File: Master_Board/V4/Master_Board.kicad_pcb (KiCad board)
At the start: 2 copper layers, 137.4 x 98.3 mm, 204 parts, among them J101 649016227222, J201 Header_Male_Pin_2.54mm_1X3_,_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, J202 Header_Male_Pin_2.54mm_1X6_,_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, J301 Header_Male_Pin_2.54mm_1X2_,_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, J401 649006227222, J701 649004227222, J702 649004227222, J703 649004227222, J704 649002227222, J801 649002227222, J802 649002227222, J901 649002227222, J902 649002227222, J903 649002227222, J904 649002227222, Q1101 BSS806NH6327XTSA1, Q1102 BSS806NH6327XTSA1, Q1103 BSS806NH6327XTSA1, Q701 BC849BLT1G, Q702 BC849BLT1G, Q703 BC849BLT1G, Q704 BC849BLT1G, Q801 BC849BLT1G, Q802 BC849BLT1G, SW201 PTS645SM43SMTR92, SW202 PTS645SM43SMTR92, U201 STM32F446RE, U301 OKI-78SR-5/1.5-W36-C, U302 AZ1117IH-3.3TRG1, U401 SN65HVD232DR, U501 SN65HVD232DR, U701 CPC1117NTR, U901 ACPL-C87A-500E, U902 NCS1S2405SC, U903 ACPL-C87A-500E, U904 LMV321RILT, U905 LMV321RILT

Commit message: Reparation of the fan circuit -no more patch require on the PSU
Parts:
- removed R1101, R1103, R1105: RC0805JR-074K7L, Resistors:R0805
- removed R1102, R1104, R1106: RC0805JR-07100KL, Resistors:R0805
- moved Q1101 1.27 mm to (110.2, 47.0), turned to 0 degrees
- moved Q1102 1.10 mm to (104.1, 47.0), turned to 0 degrees
- moved Q1103 1.10 mm to (98.0, 47.0), turned to 0 degrees
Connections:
- Q1101 pad 2: DGND -> /IO5
- Q1101 pad 3: /IO5 -> 12V
- Q1102 pad 2: DGND -> /IO7
- Q1102 pad 3: /IO7 -> 12V
- Q1103 pad 2: DGND -> /IO8
- Q1103 pad 3: /IO8 -> 12V
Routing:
- net DGND: track 687.9 -> 655.6 mm, vias 26 -> 25
- net 12V: track 152.2 -> 161.7 mm, vias 4 -> 2
- net /PC0: track 50.5 -> 48.4 mm
- net /IO5: track 36.4 -> 37.7 mm
- net /PC1: track 50.2 -> 51.3 mm
- net /IO7: track 35.2 -> 36.2 mm
- net /PC2: track 60.1 -> 60.8 mm

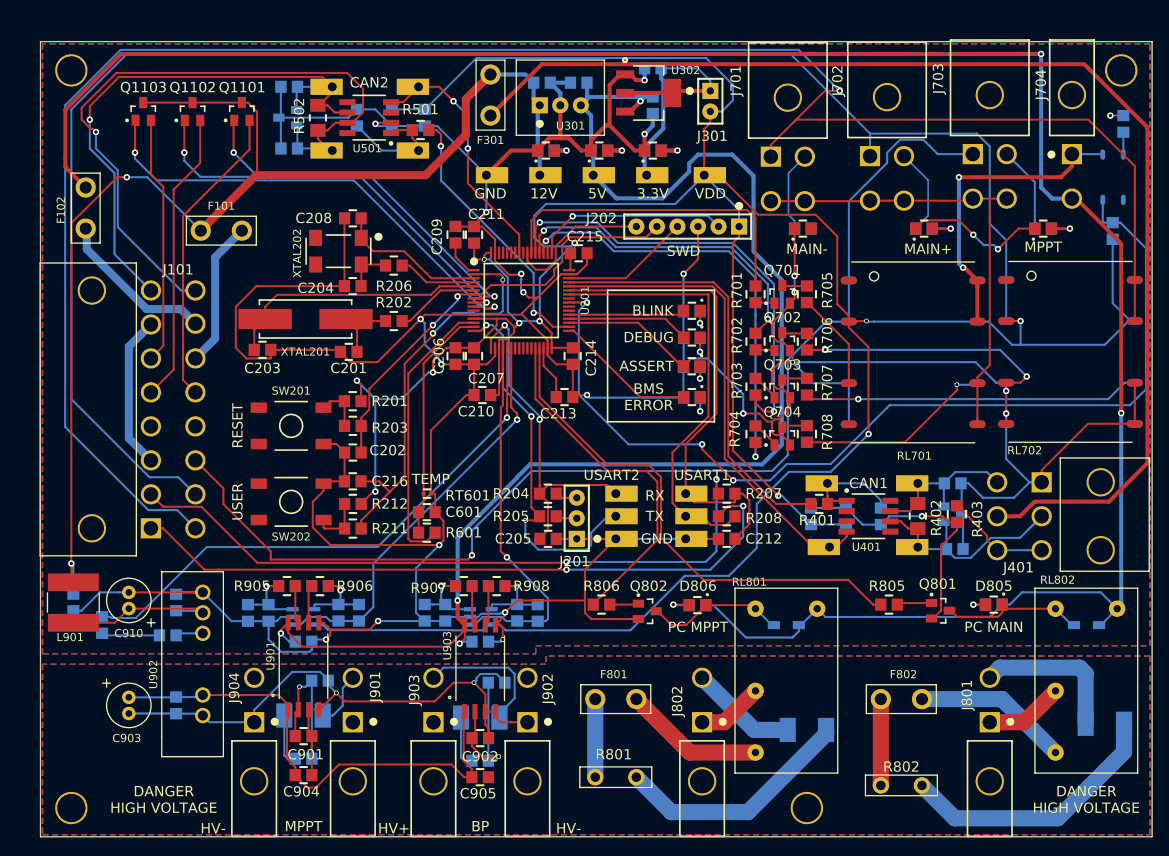
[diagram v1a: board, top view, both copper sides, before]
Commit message: Master V4 routed
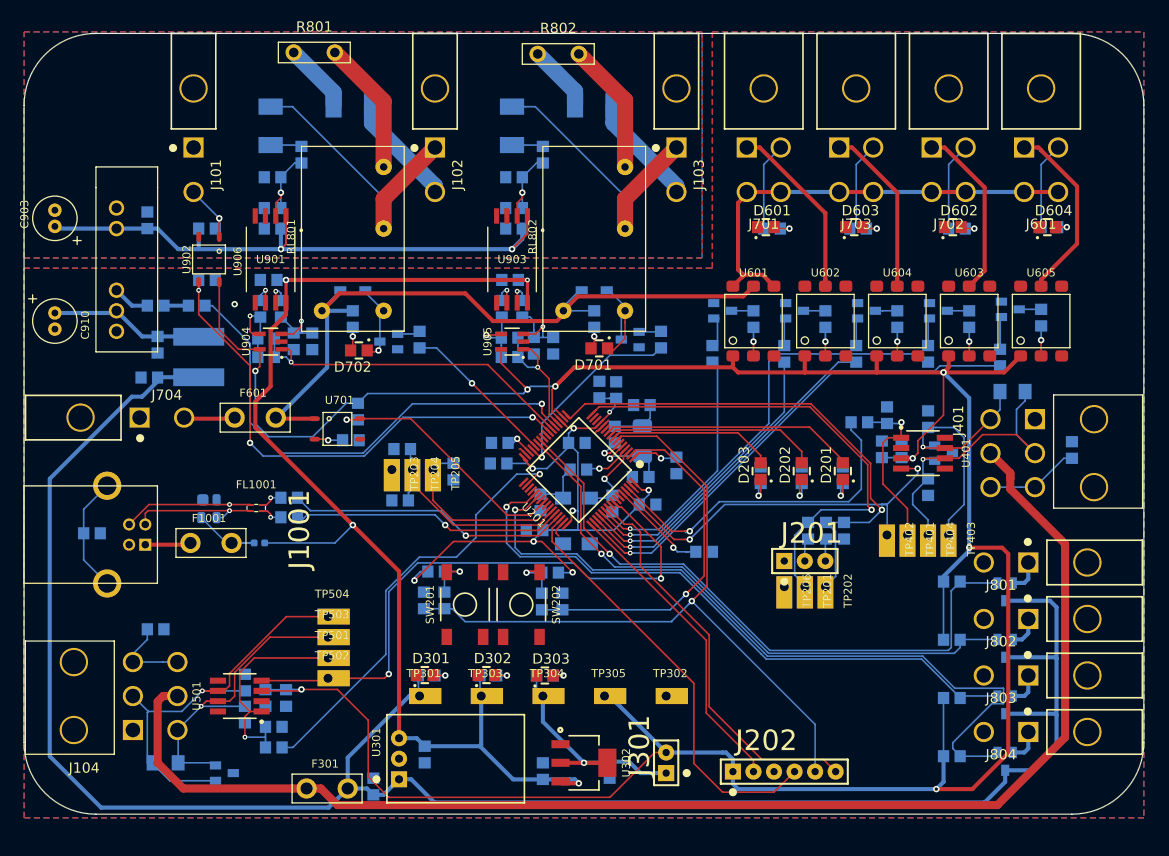
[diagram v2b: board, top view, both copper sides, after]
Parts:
- removed C601: 885012107015, Capacitors:C0805
- removed D703, D805, D806: 150080VS75000, Diodes:LED_0805_GREEN
- removed F101: 39505000440, Fuses:TE5_395
- removed F102: 39511000440, Fuses:TE5_395
- removed F801, F802: 80812000440, Fuses:TE5_395
- removed the G*** at (120.1, 75.4)
- removed J901, J902, J903, J904: 649002227222, Connectors:649002227222
- removed REF** (x4): Mounting_Hole_3mm, Connectors:Mounting_Hole_3mm
- removed RL701, RL702, RL703, RL704: CPC1907B, Relays:CPC1907B
- removed RT601: NCP15WB473F03RC, Resistors:R0402
- added D601: 150080BS75000, Diodes:LED_0805_BLUE, F.Cu at (174.0, 61.3)
- added D602: 150080BS75000, Diodes:LED_0805_BLUE, F.Cu at (197.1, 61.3)
- added D603: 150080BS75000, Diodes:LED_0805_BLUE, F.Cu at (184.9, 61.3)
- added D604: 150080BS75000, Diodes:LED_0805_BLUE, F.Cu at (208.8, 61.3)
- added F1001: 39505000440, Fuses:TE5_395, F.Cu at (106.4, 100.3)
- added F601: 39511000440, Fuses:TE5_395, F.Cu at (111.9, 84.8)
- added FB1001: 742792605, Filter:FB0603, B.Cu at (111.8, 100.3)
- added FL1001: 744230900, Filter:744230900, F.Cu at (112.0, 96.0)
- added G***: LOGO, Logo:Eclipse_logo_small_Metal, F.Cu at (184.7, 116.9)
- added J1001: 61400416121, Connectors:61400416121, F.Cu at (98.3, 98.0)
- added J102: 649002227222, Connectors:649002227222, F.Cu at (134.1, 44.1)
- added J103: 649002227222, Connectors:649002227222, F.Cu at (164.0, 44.1)
- added J104: 649006227222, Connectors:649006227222, F.Cu at (89.5, 119.3)
- added J601: 649004227222, Connectors:649004227222, F.Cu at (209.0, 44.1)
- added J803: 649002227222, Connectors:649002227222, F.Cu at (214.8, 116.7)
- added J804: 649002227222, Connectors:649002227222, F.Cu at (214.8, 123.7)
- added Q601: BC849BLT1G, IC:SOT-23-3, B.Cu at (205.2, 71.4)
- added Q803: BSS806NH6327XTSA1, IC:SOT-23-3, B.Cu at (204.6, 127.3)
- added R1002: RC0805JR-0710KL, Resistors:R0805, B.Cu at (197.0, 105.1)
- added R1003: RC0805JR-0710KL, Resistors:R0805, B.Cu at (197.0, 112.3)
- added R1004: RC0805JR-0710KL, Resistors:R0805, B.Cu at (197.0, 119.5)
- added R1005: RC0805JR-070RL, Resistors:R0805, B.Cu at (115.1, 97.2)
- added R1006: RC0805JR-070RL, Resistors:R0805, B.Cu at (115.1, 94.7)
- added R101: RC0805JR-070RL, Resistors:R0805, B.Cu at (98.6, 111.0)
- added R214: RC0805JR-0710KL, Resistors:R0805, B.Cu at (168.4, 101.4)
- added R602: RC0805FR-071K1L, Resistors:R0805, B.Cu at (209.0, 71.4)
- added R603: RC0805JR-071KL, Resistors:R0805, B.Cu at (209.0, 61.3)
- added R807: RC0805JR-0710KL, Resistors:R0805, B.Cu at (197.0, 126.7)
- added R914: RC0805JR-074K7L, Resistors:R0805, B.Cu at (104.9, 61.5)
- added R915: RC0805JR-074K7L, Resistors:R0805, B.Cu at (104.9, 67.8)
- added U601: TLP3543A(TP1,F, IC:6-SMD, F.Cu at (173.5, 72.9)
- added U602: TLP3543A(TP1,F, IC:6-SMD, F.Cu at (182.4, 72.9)
- added U603: TLP3543A(TP1,F, IC:6-SMD, F.Cu at (200.2, 72.9)
- added U604: TLP3543A(TP1,F, IC:6-SMD, F.Cu at (191.3, 72.9)
- added U605: TLP3543A(TP1,F, IC:6-SMD, F.Cu at (209.0, 72.9)
- added U906: CPC1117NTR, IC:4-SOP, F.Cu at (106.2, 65.3)
- C201, C202, C203, C204, C205, C206, C207, C208, C209, C210, C211, C212, C213, C214, C215, C216, C901, C902, C904, C905, L901, Q1101, Q1102, Q1103, Q701, Q702, Q703, Q704, Q801, Q802, R201, R202, R203, R204, R205, R206, R207, R208, R211, R212, R401, R402, R403, R501, R502, R701, R702, R703, R704, R705, R706, R707, R708, R805, R806, R905, R906, R907, R908, XTAL202: moved to B.Cu
- D1001: value 150080RS75000 -> 8240026; footprint Diodes:LED_0805_RED -> Diodes:SOT-143-4; moved to B.Cu
- D301, D302, D303, D701, D702: value 150080VS75000 -> 150080BS75000; footprint Diodes:LED_0805_GREEN -> Diodes:LED_0805_BLUE
- J101: value 649016227222 -> 649002227222; footprint Connectors:649016227222 -> Connectors:649002227222
- R1001: value RC0805JR-07330RL -> RC0805JR-070RL
- R601: value RC0805JR-0733KL -> RC0805JR-0710KL; moved to B.Cu
- U301: value OKI-78SR-5/1.5-W36-C -> OKI-78SR-5_1.5-W36H-C; footprint Assembly:OKI-78SR_Vertical -> Assembly:OKI-78SR_Horizontal
- U701, U904, U905: moved to F.Cu
- XTAL201: value ABLS-8.000MHZ-D-T -> 7A-8.000MAHJ-T; footprint Crystals:HC49_US -> Crystals:TXC_7A_Series; moved to B.Cu
- moved Q1103 129.4 mm to (204.6, 120.3)
- moved J704 128.9 mm to (90.3, 84.8), turned to 270 degrees
- moved Q1102 120.4 mm to (204.6, 113.4)
- moved Q1101 111.5 mm to (204.6, 106.4)
- moved R712 103.8 mm to (122.7, 87.6), turned to 0 degrees
- moved U701 100.8 mm to (122.0, 86.2), turned to 0 degrees
- moved R802 99.9 mm to (149.4, 39.9), turned to 0 degrees
- moved D802 99.1 mm to (153.8, 46.2), turned to 0 degrees
- moved R801 97.0 mm to (119.2, 39.7), turned to 0 degrees
- moved R713 95.5 mm to (124.6, 83.1), turned to 270 degrees
- moved D801 95.5 mm to (124.0, 46.2), turned to 0 degrees
- moved C301 88.7 mm to (126.5, 129.4), turned to 270 degrees
- moved F301 88.1 mm to (120.8, 130.7), turned to 0 degrees
- moved C304 87.9 mm to (155.7, 129.4), turned to 90 degrees
- moved C302 86.0 mm to (132.8, 127.5), turned to 90 degrees
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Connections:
- net /Voltage Sense/5V_ISO renamed 5V_HP
- D1001 pad 1: Net-(D1001-Pad1) -> DGND
- D1001 pad 2: /PB12 -> (no net)
- D201 pad 2: /PC6 -> /PC2
- D202 pad 2: /PB15 -> /PC1
- D203 pad 2: /PB14 -> /PC0
- D701 pad 1: DGND -> Net-(D701-Pad1)
- D702 pad 1: DGND -> Net-(D702-Pad1)
- D801 pad 2: Net-(D801-Pad2) -> /HV_Mppt+
- D802 pad 2: Net-(D802-Pad2) -> /HV_High_Side+
- D803 pad 1: /Contactor_12V -> /12V_Mush
- D803 pad 2: Net-(D803-Pad2) -> Net-(D701-Pad1)
- D804 pad 1: /Contactor_12V -> /12V_Mush
- D804 pad 2: Net-(D804-Pad2) -> Net-(D702-Pad1)
- D901 pad 2: Net-(D901-Pad2) -> /HV_Mppt-
- D902 pad 2: Net-(D902-Pad2) -> /HV_High_Side-
- J101 pad 1: /RS232_TX -> AGND
- J101 pad 2: /RS232_RX -> /HV_Low_Side+
- J101 pad 3: /GND -> (no net)
- J701 pad 1: /IO2 -> Net-(J701-Pad1)
- J702 pad 1: /IO1 -> Net-(J702-Pad1)
- J703 pad 1: /IO3 -> Net-(J703-Pad1)
- J704 pad 1: /ContactorControl/12V_Protected -> DGND
- J704 pad 2: /Contactor_12V -> Net-(F601-Pad1)
- J801 pad 2: Net-(D802-Pad2) -> DGND
- J802 pad 2: Net-(D801-Pad2) -> DGND
- Q1101 pad 1: /PC0 -> /PB0
- Q1101 pad 2: /IO5 -> Net-(J801-Pad1)
- Q1102 pad 1: /PC1 -> /PB1
- Q1102 pad 2: /IO7 -> Net-(J802-Pad1)
- Q1103 pad 1: /PC2 -> /PC6
- Q1103 pad 2: /IO8 -> Net-(J803-Pad1)
- Q801 pad 3: Net-(D803-Pad2) -> Net-(D701-Pad1)
- Q802 pad 3: Net-(D804-Pad2) -> Net-(D702-Pad1)
- R1001 pad 1: DGND -> /USB/Shield_Connector
- R1001 pad 2: Net-(D1001-Pad1) -> DGND
- R401 pad 1: /PA12 -> /PB9
- R601 pad 1: /NTC_1_ADC -> /PA15
- R601 pad 2: /NTC_1_GPIO -> Net-(Q601-Pad1)
- R709 pad 2: Net-(D701-Pad2) -> Net-(D601-Pad2)
- R710 pad 2: Net-(D702-Pad2) -> Net-(D602-Pad2)
- R801 pad 2: Net-(F801-Pad1) -> Net-(R801-Pad2)
- R802 pad 2: Net-(F802-Pad1) -> Net-(R802-Pad2)
- R803 pad 1: /Contactor_12V -> /12V_Mush
- R803 pad 2: Net-(D805-Pad2) -> Net-(D701-Pad2)
- R804 pad 1: /Contactor_12V -> /12V_Mush
- R804 pad 2: Net-(D806-Pad2) -> Net-(D702-Pad2)
- RL801 pad 1: /Contactor_12V -> /12V_Mush
- RL801 pad 2: Net-(D804-Pad2) -> Net-(D702-Pad1)
- RL801 pad 3: Net-(J802-Pad1) -> /HV_Mppt-
- RL801 pad 4: Net-(F801-Pad2) -> Net-(R801-Pad2)
- RL802 pad 1: /Contactor_12V -> /12V_Mush
- RL802 pad 2: Net-(D803-Pad2) -> Net-(D701-Pad1)
- RL802 pad 3: Net-(J801-Pad1) -> /HV_High_Side-
- RL802 pad 4: Net-(F802-Pad2) -> Net-(R802-Pad2)
- TP402 pad 1: /PA11 -> /PB8
- U201 pad 14: /NTC_1_GPIO -> /PA0
- U201 pad 15: /NTC_1_ADC -> /PA1
- U401 pad 4: /PA11 -> /PB8
- U701 pad 1: /ContactorControl/12V_Protected -> /12V_Mush
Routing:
- net DGND: track 655.6 -> 8.39 mm, vias 25 -> 1
- net /Contactor_12V: track 268.3 -> 0.00 mm, vias 2 -> 0
- net /IO2: track 238.2 -> 0.00 mm, vias 1 -> 0
- net /IO1: track 202.4 -> 0.00 mm
- net /IO3: track 143.3 -> 0.00 mm, vias 1 -> 0
- net /12V_Mush: track 0.00 -> 93.5 mm
- net /PC7: track 0.00 -> 92.8 mm, vias 0 -> 1
- net /PC9: track 120.5 -> 31.4 mm, vias 3 -> 1
- net 12V: track 161.7 -> 248.4 mm, vias 2 -> 0
- net /RS232_RX: track 84.8 -> 0.00 mm, vias 2 -> 0
- net /RS232_TX: track 84.5 -> 0.00 mm, vias 2 -> 0
- net AGND: track 80.5 -> 0.00 mm, vias 2 -> 0
- net /PB0: track 0.00 -> 78.1 mm, vias 0 -> 1
- net /PB1: track 0.00 -> 72.2 mm, vias 0 -> 1
- net /PA7: track 0.00 -> 64.2 mm, vias 0 -> 3
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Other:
- board size 137.4 x 98.3 mm -> 138.4 x 96.5 mm
- board text removed: "(c) 2018 - Eclipse X"
- board text removed: "12V"
- board text removed: "3.3V"
- board text removed: "5V"
- board text removed: "ASSERT"
- board text removed: "BLINK"
- board text removed: "BMS ERROR"
- board text removed: "BMS Master Board V3"
- board text removed: "BP"
- board text removed: "CAN1"
- board text removed: "CAN2"
- board text removed: "DANGER HIGH VOLTAGE"
- board text removed: "DEBUG"
- board text removed: "GND"
- board text removed: "HV+"
- board text removed: "HV-"
- board text removed: "Julien Bourassa/Pierre-Olivier Meilleur"
- board text removed: "MAIN+"
- board text removed: "MAIN-"
- board text removed: "MPPT"
- board text removed: "PC MAIN"
- board text removed: "PC MPPT"
- board text removed: "RESET"
- board text removed: "RX"
- board text removed: "SWD"
- board text removed: "TEMP"
- board text removed: "TX"
- board text removed: "USART1"
- board text removed: "USART2"
- board text removed: "USER"
- board text removed: "VDD"

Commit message: Repair USB ESD protection net
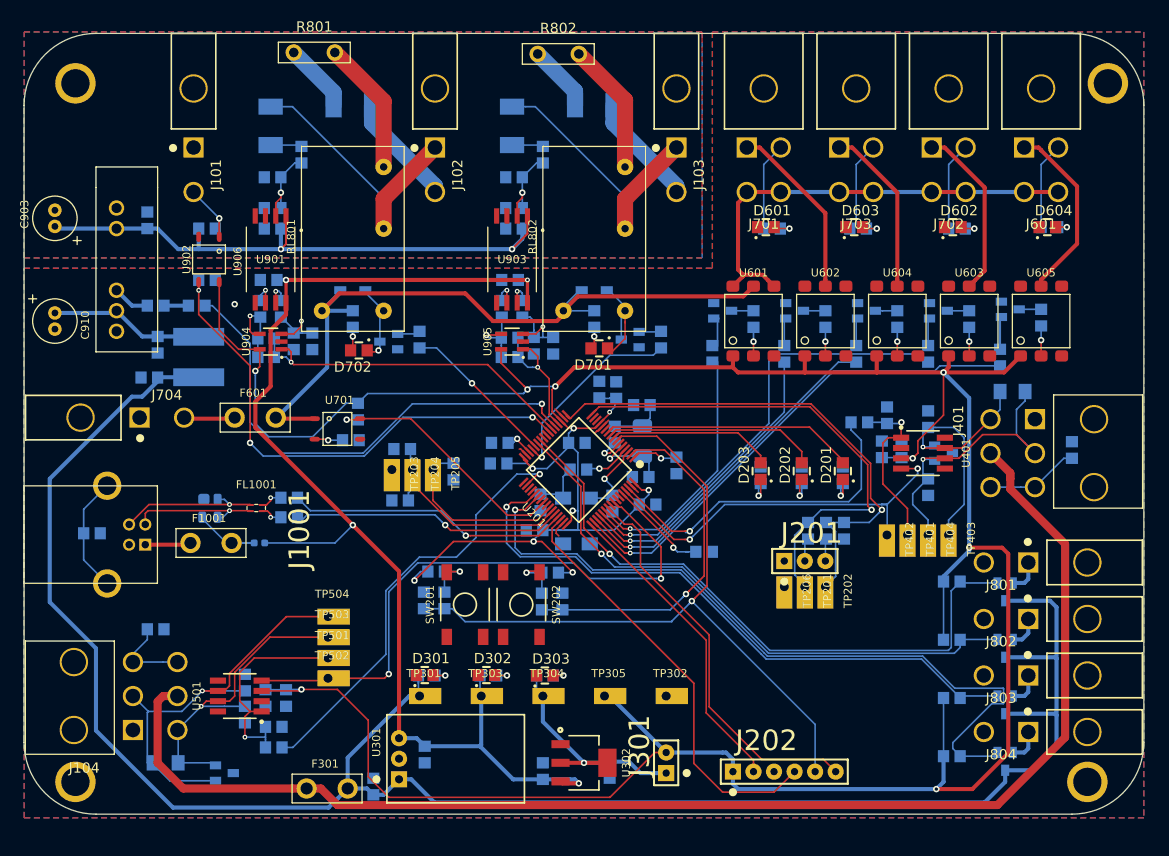
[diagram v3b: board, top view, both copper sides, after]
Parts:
- added H101: Mounting-Hole-M3, Connectors:Mounting_Hole_3mm, F.Cu at (214.8, 129.9)
- added H102: Mounting-Hole-M3, Connectors:Mounting_Hole_3mm, F.Cu at (89.7, 129.9)
- added H103: Mounting-Hole-M3, Connectors:Mounting_Hole_3mm, F.Cu at (217.3, 43.5)
- added H104: Mounting-Hole-M3, Connectors:Mounting_Hole_3mm, F.Cu at (89.7, 43.5)
- moved D1001 0.14 mm to (105.5, 94.9)
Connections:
- D1001 pad 2: (no net) -> /USB/D+
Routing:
- net 12V: track 248.4 -> 243.2 mm
- net /USB/D+: track 16.7 -> 18.4 mm
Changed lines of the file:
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@@
     (thickness 1.6)
     (drawings 8)
-    (tracks 1207)
+    (tracks 1211)
     (zones 0)
-    (modules 212)
-    (nets 172)
+    (modules 216)
+    (nets 176)
   )
   (page A4)
@@
   (net 170 "Net-(D701-Pad1)")
   (net 171 "Net-(D702-Pad1)")
+  (net 172 "Net-(H101-Pad1)")
+  (net 173 "Net-(H102-Pad1)")
+  (net 174 "Net-(H103-Pad1)")
+  (net 175 "Net-(H104-Pad1)")
   (net_class Default "Ceci est la Netclass par défaut"
     (clearance 0.1524)
@@
     (add_net "Net-(FL1001-Pad2)")
     (add_net "Net-(FL1001-Pad3)")
+    (add_net "Net-(H101-Pad1)")
+    (add_net "Net-(H102-Pad1)")
+    (add_net "Net-(H103-Pad1)")
+    (add_net "Net-(H104-Pad1)")
     (add_net "Net-(J601-Pad1)")
     (add_net "Net-(J601-Pad2)")
@@
     )
   )
-  (module Diodes:SOT-143-4 (layer B.Cu)
-    (at 105.41 94.996)
-    (fp_text reference D1001 (at 1.905 3.81) (layer B.SilkS)
-      (effects (font (size 1 1) (thickness 0.15)) (justify mirror))
-    )
-    (fp_text value 8240026 (at 1.27 5.08) (layer B.Fab)
-      (effects (font (size 1 1) (thickness 0.15)) (justify mirror))
-    )
-    (fp_circle (center 0 -1.27) (end 0.1 -1.27) (layer B.SilkS) (width 0.3))
-    (pad 4 smd roundrect (at -0.2 2.2) (size 1 1.4) (layers B.Cu B.Paste B.Mask) (roundrect_rratio 0.25)
-      (net 137 "Net-(D1001-Pad4)"))
-    (pad 3 smd roundrect (at 1.7 2.2) (size 1 1.4) (layers B.Cu B.Paste B.Mask) (roundrect_rratio 0.25)
-      (net 141 /USB/D-))
-    (pad 2 smd roundrect (at 1.7 0) (size 1 1.4) (layers B.Cu B.Paste B.Mask) (roundrect_rratio 0.25))
-    (pad 1 smd roundrect (at 0 0) (size 1.4 1.4) (layers B.Cu B.Paste B.Mask) (roundrect_rratio 0.25)
-      (net 1 DGND))
-    (model ${KISYS3DMOD}/Diodes/SOT143-4L.stp
-      (offset (xyz 0.75 1 0.5))
-      (scale (xyz 1 1 1))
-      (rotate (xyz 0 0 0))
-    )
-  )
   (module Crystals:TXC_7A_Series (layer B.Cu)
     (at 159.749164 87.731638 90)
@@
       (xy 0.952035 0.4064) (xy 1.036532 0.406546)) (layer F.Mask) (width 0.01))
   )
+  (module Connectors:Mounting_Hole_3mm (layer F.Cu)
+    (at 214.757 129.868184)
+    (fp_text reference H101 (at 0 -3.302) (layer F.SilkS) hide
+      (effects (font (size 1.27 1.27) (thickness 0.2032)))
+    )
+    (fp_text value Mounting-Hole-M3 (at 0 3.683) (layer F.Fab) hide
+      (effects (font (size 1.27 1.27) (thickness 0.2032)))
+    )
+    (pad 1 thru_hole circle (at 0 0) (size 5 5) (drill 3.5) (layers *.Cu *.Mask)
+      (net 172 "Net-(H101-Pad1)"))
+  )
+  (module Connectors:Mounting_Hole_3mm (layer F.Cu)
+    (at 89.662 129.868184)
+    (fp_text reference H102 (at 0 -3.302) (layer F.SilkS) hide
+      (effects (font (size 1.27 1.27) (thickness 0.2032)))
+    )
+    (fp_text value Mounting-Hole-M3 (at 0 3.683) (layer F.Fab) hide
+      (effects (font (size 1.27 1.27) (thickness 0.2032)))
+    )
+    (pad 1 thru_hole circle (at 0 0) (size 5 5) (drill 3.5) (layers *.Cu *.Mask)
+      (net 173 "Net-(H102-Pad1)"))
+  )
+  (module Connectors:Mounting_Hole_3mm (layer F.Cu)
+    (at 217.297 43.508184)
+    (fp_text reference H103 (at 0 -3.302) (layer F.SilkS) hide
+      (effects (font (size 1.27 1.27) (thickness 0.2032)))
+    )
+    (fp_text value Mounting-Hole-M3 (at 0 3.683) (layer F.Fab) hide
+      (effects (font (size 1.27 1.27) (thickness 0.2032)))
+    )
+    (pad 1 thru_hole circle (at 0 0) (size 5 5) (drill 3.5) (layers *.Cu *.Mask)
+      (net 174 "Net-(H103-Pad1)"))
+  )
+  (module Connectors:Mounting_Hole_3mm (layer F.Cu)
+    (at 89.662 43.508184)
+    (fp_text reference H104 (at 0 -3.302) (layer F.SilkS) hide
+      (effects (font (size 1.27 1.27) (thickness 0.2032)))
+    )
+    (fp_text value Mounting-Hole-M3 (at 0 3.683) (layer F.Fab) hide
+      (effects (font (size 1.27 1.27) (thickness 0.2032)))
+    )
+    (pad 1 thru_hole circle (at 0 0) (size 5 5) (drill 3.5) (layers *.Cu *.Mask)
+      (net 175 "Net-(H104-Pad1)"))
+  )
+  (module Diodes:SOT-143-4 (layer B.Cu)
+    (at 105.537 94.943184)
+    (fp_text reference D1001 (at 1.905 3.81) (layer B.SilkS)
+      (effects (font (size 1 1) (thickness 0.15)) (justify mirror))
+    )
+    (fp_text value 8240026 (at 1.27 5.08) (layer B.Fab)
+      (effects (font (size 1 1) (thickness 0.15)) (justify mirror))
+    )
+    (fp_circle (center 0 -1.27) (end 0.1 -1.27) (layer B.SilkS) (width 0.3))
+    (pad 1 smd roundrect (at 0 0) (size 1.4 1.4) (layers B.Cu B.Paste B.Mask) (roundrect_rratio 0.25)
+      (net 1 DGND))
+    (pad 2 smd roundrect (at 1.7 0) (size 1 1.4) (layers B.Cu B.Paste B.Mask) (roundrect_rratio 0.25)
+      (net 142 /USB/D+))
+    (pad 3 smd roundrect (at 1.7 2.2) (size 1 1.4) (layers B.Cu B.Paste B.Mask) (roundrect_rratio 0.25)
+      (net 141 /USB/D-))
+    (pad 4 smd roundrect (at -0.2 2.2) (size 1 1.4) (layers B.Cu B.Paste B.Mask) (roundrect_rratio 0.25)
+      (net 137 "Net-(D1001-Pad4)"))
+    (model ${KISYS3DMOD}/Diodes/SOT143-4L.stp
+      (offset (xyz 0.75 1 0.5))
+      (scale (xyz 1 1 1))
+      (rotate (xyz 0 0 0))
+    )
+  )
   (gr_arc (start 212.852 124.968) (end 212.852 133.858) (angle -90) (layer Edge.Cuts) (width 0.1))
   (gr_arc (start 92.202 124.968) (end 83.312 124.968) (angle -90) (layer Edge.Cuts) (width 0.1))
@@
   (segment (start 210.947 125.423184) (end 210.947 121.613184) (width 0.508) (layer B.Cu) (net 13))
   (segment (start 210.947 121.613184) (end 210.947 114.628184) (width 0.508) (layer B.Cu) (net 13))
-  (segment (start 122.067001 131.932999) (end 123.317 130.683) (width 0.508) (layer B.Cu) (net 13))
   (segment (start 120.956816 133.043184) (end 122.067001 131.932999) (width 0.508) (layer B.Cu) (net 13))
-  (segment (start 99.822 80.338184) (end 97.917 82.243184) (width 0.508) (layer B.Cu) (net 13))
+  (segment (start 101.727 133.043184) (end 120.956816 133.043184) (width 0.508) (layer B.Cu) (net 13))
+  (segment (start 92.202 123.518184) (end 101.727 133.043184) (width 0.508) (layer B.Cu) (net 13))
+  (segment (start 122.067001 131.932999) (end 123.317 130.683) (width 0.508) (layer B.Cu) (net 13))
+  (segment (start 92.202 113.358184) (end 92.202 123.518184) (width 0.508) (layer B.Cu) (net 13))
+  (segment (start 97.917 82.243184) (end 96.647 82.243184) (width 0.508) (layer B.Cu) (net 13))
   (segment (start 99.822 79.883) (end 99.822 80.338184) (width 0.508) (layer B.Cu) (net 13))
+  (segment (start 86.487 107.643184) (end 92.202 113.358184) (width 0.508) (layer B.Cu) (net 13))
+  (segment (start 99.822 80.338184) (end 97.917 82.243184) (width 0.508) (layer B.Cu) (net 13))
   (segment (start 96.647 82.243184) (end 86.487 92.403184) (width 0.508) (layer B.Cu) (net 13))
-  (segment (start 86.487 126.693184) (end 92.837 133.043184) (width 0.508) (layer B.Cu) (net 13))
-  (segment (start 97.917 82.243184) (end 96.647 82.243184) (width 0.508) (layer B.Cu) (net 13))
-  (segment (start 92.837 133.043184) (end 120.956816 133.043184) (width 0.508) (layer B.Cu) (net 13))
-  (segment (start 86.487 92.403184) (end 86.487 126.693184) (width 0.508) (layer B.Cu) (net 13))
+  (segment (start 86.487 92.403184) (end 86.487 107.643184) (width 0.508) (layer B.Cu) (net 13))
   (via (at 115.697 67.818) (size 0.8) (drill 0.4) (layers F.Cu B.Cu) (net 14))
   (segment (start 114.572 67.818) (end 115.697 67.818) (width 0.4) (layer B.Cu) (net 14))
@@
   (segment (start 108.712 95.578184) (end 111.230184 95.578184) (width 0.2) (layer F.Cu) (net 142))
   (via (at 108.712 95.578184) (size 0.6) (drill 0.3) (layers F.Cu B.Cu) (net 142))
+  (segment (start 108.077 94.943184) (end 108.712 95.578184) (width 0.2032) (layer B.Cu) (net 142))
+  (segment (start 107.237 94.943184) (end 108.077 94.943184) (width 0.2032) (layer B.Cu) (net 142))
   (via (at 107.442 60.198) (size 0.8) (drill 0.4) (layers F.Cu B.Cu) (net 143))
   (segment (start 107.442 62.478) (end 107.442 60.198) (width 0.254) (layer F.Cu) (net 143))
